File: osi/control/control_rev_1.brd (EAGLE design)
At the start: 25.4 x 25.4 mm, 8 parts, among them IC1 TINY24/44/84-PU

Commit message: control brain
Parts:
- removed C1: (no value), SparkFun:CAP-PTH-SMALL-KIT
- removed IC1: TINY24/44/84-PU, avr-7:DIL14
- removed IC2_L, IC2_R: (no value), SparkFun_mod:1X05
- removed U$1: PTS635_SWITCH, _my-parts:PTS635_SWITCH
- added C2: 100uF/6V, rcl-ez:E2,5-5
- added C6: 0.1uF, rcl-ez:C025-025X050
- added C7: 100uF/16V, rcl-ez:E2,5-6
- added J1, J2: 1X2-3.5MM, adafruit_mod:1X2-3.5MM
- added R2: (no value), adafruit_mod:0204V
- added TRACKS: L293D, texas:DIL16
- moved R1 6.35 mm to (14.0, 20.3), turned to 90 degrees
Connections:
- removed net D8: IC1.5, R1.1
- removed net RESET: IC1.4, U$1.P$2
- new net N$1: J1.2, TRACKS.3
- new net N$2: J2.2, TRACKS.14
- new net N$3: J1.1, TRACKS.6
- new net N$4: J2.1, TRACKS.11
- new net N$5: TRACKS.9
- new net N$6: R1.1
- new net N$7: R2.1
- new net VCC: C2.+, C6.1, TRACKS.16
- net +3V3: no longer C1.2, IC1.1, IC2_L.4, IC2_R.2
- net +5V: no longer IC2_L.5, IC2_R.1
- net AREF_D0: now also TRACKS.2; no longer IC1.13
- net D1: now also TRACKS.7; no longer IC1.12
- net D10: now also TRACKS.15; no longer IC1.2
- net D2: now also R2.2; no longer IC1.11
- net D3: now also R1.2; no longer IC1.10
- net D5: now also TRACKS.1; no longer IC1.8
- net D7: no longer IC1.6
- net D9: now also TRACKS.10; no longer IC1.3
- net GND: now also C2.-, C6.2, C7.-, TRACKS.12, TRACKS.13, TRACKS.4, TRACKS.5; no longer C1.1, IC1.14, IC2_L.3, IC2_R.3, R1.2, U$1.P$1
- net SCL_D4: no longer IC1.9, IC2_L.1, IC2_R.5
- net SDA_D6: no longer IC1.7, IC2_L.2, IC2_R.4
- net V+: now also C7.+, TRACKS.8
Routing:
- net +3V3: track 39.4 -> 0.00 mm
- net +5V: track 39.0 -> 0.00 mm
- net SDA_D6: track 37.0 -> 0.00 mm
- net SCL_D4: track 34.8 -> 0.00 mm
- net N$3: track 0.00 -> 26.3 mm
- net N$2: track 0.00 -> 21.8 mm
- net V+: track 0.00 -> 20.3 mm
- net VCC: track 0.00 -> 17.3 mm
- net D5: track 4.34 -> 20.9 mm
- net RESET: track 16.3 -> 0.00 mm
- net D7: track 14.1 -> 0.00 mm
- net D2: track 16.8 -> 3.07 mm
- net N$4: track 0.00 -> 13.6 mm
- net AREF_D0: track 25.9 -> 14.4 mm
- net D8: track 9.20 -> 0.00 mm
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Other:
- board text added: "CONTROL"
- board text added: "Control Rev 1 Feb 12"
- board text added: "L293D"
- board text removed: "3V3"
- board text removed: "Attiny 84"
- board text removed: "BRAIN"
- board text removed: "Brain Rev 1 Feb 12"
- board text removed: "RESET"
- board text removed: "SCK"
- board text removed: "SDA"

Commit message: update
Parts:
- added LED1, LED2: (no value), adafruit:LED3MM
- added R3, R4: (no value), adafruit_mod:0204V
- moved C6 1.97 mm to (22.9, 2.41)
- moved TRACKS 1.90 mm to (15.2, 8.89)
- moved C2 0.25 mm to (15.2, 16.3), turned to 90 degrees
- turned J1 to 180 degrees
- turned J2 to 180 degrees
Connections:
- net AREF_D0: now also LED1.A
- net D1: now also R3.1
- net D10: now also LED2.A
- net D9: now also R4.1
- net GND: now also R1.1, R2.1
- net N$1: now also J1.1; no longer J1.2
- net N$3: now also J1.2; no longer J1.1
- net N$6: now also LED1.K, R3.2; no longer R1.1
- net N$7: now also LED2.K, R4.2; no longer R2.1
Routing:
- net AREF_D0: track 14.4 -> 38.1 mm
- net N$7: track 0.00 -> 20.9 mm
- net D10: track 7.67 -> 24.4 mm
- net N$6: track 0.00 -> 11.3 mm
- net D9: track 6.40 -> 17.3 mm
- net V+: track 20.3 -> 27.1 mm
- net N$3: track 26.3 -> 21.9 mm
- net N$4: track 13.6 -> 17.2 mm
- net D5: track 20.9 -> 23.2 mm
- net D1: track 20.7 -> 19.6 mm
- net N$1: track 6.22 -> 5.19 mm
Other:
- board text added: "A"
- board text added: "B"
- board text added: "Rev 1 Feb 12"
- board text removed: "Control Rev 1 Feb 12"

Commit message: chuck
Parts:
- removed R1, R2: (no value), adafruit_mod:0204V
- moved JP8 1.27 mm to (6.35, 24.1)
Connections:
- removed net D2: JP8.6, R2.2
- removed net D3: JP8.5, R1.2
- net GND: now also JP8.5, JP8.6; no longer R1.1, R2.1
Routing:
- net D3: track 3.07 -> 0.00 mm
- net D2: track 3.07 -> 0.00 mm
- net AREF_D0: track 38.1 -> 38.8 mm
- net D5: track 23.2 -> 22.5 mm
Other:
- board text removed: "D4"
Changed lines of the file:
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@@
 <setting verticaltext="up"/>
 </settings>
-<grid distance="0.01" unitdist="inch" unit="inch" style="lines" multiple="1" display="yes" altdistance="0.005" altunitdist="inch" altunit="inch"/>
+<grid distance="0.05" unitdist="inch" unit="inch" style="lines" multiple="1" display="yes" altdistance="0.005" altunitdist="inch" altunit="inch"/>
 <layers>
 <layer number="1" name="Top" color="4" fill="1" visible="yes" active="yes"/>
@@
 <text x="12.192" y="2.413" size="1.016" layer="22" font="vector" ratio="15" rot="MR0">D9</text>
 <text x="15.367" y="2.413" size="1.016" layer="22" font="vector" ratio="15" rot="MR0">D10</text>
-<text x="23.622" y="21.971" size="1.016" layer="22" font="vector" ratio="15" rot="MR0">D0</text>
-<text x="21.082" y="21.971" size="1.016" layer="22" font="vector" ratio="15" rot="MR0">D1</text>
-<text x="18.923" y="21.971" size="1.016" layer="22" font="vector" ratio="15" rot="MR0">D2</text>
-<text x="16.002" y="22.098" size="1.016" layer="22" font="vector" ratio="15" rot="MR0">D3</text>
-<text x="13.081" y="21.971" size="1.016" layer="22" font="vector" ratio="15" rot="MR0">D4</text>
-<text x="10.922" y="21.971" size="1.016" layer="22" font="vector" ratio="15" rot="MR0">D5</text>
-<text x="8.382" y="21.971" size="1.016" layer="22" font="vector" ratio="15" rot="MR0">D6</text>
-<text x="5.842" y="21.971" size="1.016" layer="22" font="vector" ratio="15" rot="MR0">D7</text>
-<text x="4.191" y="21.59" size="1.016" layer="21" font="vector" ratio="15">D7</text>
-<text x="6.731" y="21.59" size="1.016" layer="21" font="vector" ratio="15">D6</text>
-<text x="9.271" y="21.59" size="1.016" layer="21" font="vector" ratio="15">D5</text>
-<text x="12.065" y="21.844" size="0.8128" layer="21" font="vector" ratio="15">D4</text>
-<text x="14.605" y="21.844" size="0.8128" layer="21" font="vector" ratio="15">D3</text>
-<text x="17.145" y="21.844" size="0.8128" layer="21" font="vector" ratio="15">D2</text>
-<text x="19.685" y="21.59" size="1.016" layer="21" font="vector" ratio="15">D1</text>
-<text x="22.098" y="21.59" size="1.016" layer="21" font="vector" ratio="15">D0</text>
+<text x="24.892" y="21.971" size="1.016" layer="22" font="vector" ratio="15" rot="MR0">D0</text>
+<text x="22.352" y="21.971" size="1.016" layer="22" font="vector" ratio="15" rot="MR0">D1</text>
+<text x="20.193" y="21.971" size="1.016" layer="22" font="vector" ratio="15" rot="MR0">D2</text>
+<text x="12.192" y="21.971" size="1.016" layer="22" font="vector" ratio="15" rot="MR0">D5</text>
+<text x="9.652" y="21.971" size="1.016" layer="22" font="vector" ratio="15" rot="MR0">D6</text>
+<text x="7.112" y="21.971" size="1.016" layer="22" font="vector" ratio="15" rot="MR0">D7</text>
+<text x="5.461" y="21.59" size="1.016" layer="21" font="vector" ratio="15">D7</text>
+<text x="8.001" y="21.59" size="1.016" layer="21" font="vector" ratio="15">D6</text>
+<text x="10.541" y="21.59" size="1.016" layer="21" font="vector" ratio="15">D5</text>
+<text x="15.875" y="21.844" size="0.8128" layer="21" font="vector" ratio="15">D3</text>
+<text x="18.415" y="21.844" size="0.8128" layer="21" font="vector" ratio="15">D2</text>
+<text x="20.955" y="21.59" size="1.016" layer="21" font="vector" ratio="15">D1</text>
+<text x="23.368" y="21.59" size="1.016" layer="21" font="vector" ratio="15">D0</text>
 <text x="0.508" y="2.794" size="1.016" layer="21" font="vector" ratio="15">V+</text>
 <text x="2.54" y="2.794" size="0.8128" layer="21" font="vector" ratio="15">GND</text>
@@
 <elements>
 <element name="JP6" library="SparkFun" package="1X06" value="" x="1.27" y="1.27"/>
-<element name="JP8" library="SparkFun" package="1X08" value="" x="5.08" y="24.13"/>
+<element name="JP8" library="SparkFun" package="1X08" value="" x="6.35" y="24.13"/>
 <element name="TRACKS" library="texas" package="DIL16" value="L293D" x="15.24" y="8.89" rot="R180"/>
 <element name="C7" library="rcl-ez" package="E2,5-6" value="100uF/16V" x="10.16" y="18.415"/>
@@
 <element name="J1" library="adafruit_mod" package="1X2-3.5MM" value="1X2-3.5MM" x="21.59" y="17.78" rot="R180"/>
 <element name="J2" library="adafruit_mod" package="1X2-3.5MM" value="1X2-3.5MM" x="3.81" y="17.78" rot="R180"/>
-<element name="R1" library="adafruit_mod" package="0204V" value="" x="13.97" y="20.32" rot="R90"/>
-<element name="R2" library="adafruit_mod" package="0204V" value="" x="16.51" y="20.32" rot="R90"/>
 <element name="LED1" library="adafruit" package="LED3MM" value="" x="2.54" y="12.065" rot="R90"/>
 <element name="LED2" library="adafruit" package="LED3MM" value="" x="2.54" y="7.366" rot="R90"/>
@@
 <contactref element="TRACKS" pad="5"/>
 <contactref element="TRACKS" pad="4"/>
-<contactref element="R1" pad="1"/>
-<contactref element="R2" pad="1"/>
+<contactref element="JP8" pad="5"/>
+<contactref element="JP8" pad="6"/>
 </signal>
 <signal name="SDA_D6">
@@
 <wire x1="6.35" y1="13.208" x2="6.35" y2="12.7" width="0.6096" layer="16"/>
 </signal>
-<signal name="D3">
-<contactref element="JP8" pad="5"/>
-<contactref element="R1" pad="2"/>
-<wire x1="15.24" y1="24.13" x2="15.24" y2="22.86" width="0.4064" layer="16"/>
-<wire x1="15.24" y1="22.86" x2="13.97" y2="21.59" width="0.4064" layer="16"/>
-</signal>
-<signal name="D2">
-<contactref element="JP8" pad="6"/>
-<contactref element="R2" pad="2"/>
-<wire x1="17.78" y1="24.13" x2="17.78" y2="22.86" width="0.4064" layer="16"/>
-<wire x1="17.78" y1="22.86" x2="16.51" y2="21.59" width="0.4064" layer="16"/>
-</signal>
 <signal name="D1">
 <contactref element="JP8" pad="7"/>
 <contactref element="TRACKS" pad="7"/>
-<wire x1="20.32" y1="24.13" x2="20.32" y2="21.59" width="0.3048" layer="16"/>
-<wire x1="20.32" y1="21.59" x2="18.034" y2="20.32" width="0.3048" layer="16"/>
+<wire x1="21.59" y1="24.13" x2="21.59" y2="23.495" width="0.3048" layer="16"/>
+<wire x1="21.59" y1="23.495" x2="18.034" y2="20.32" width="0.3048" layer="16"/>
 <wire x1="18.034" y1="20.32" x2="13.462" y2="20.32" width="0.3048" layer="16"/>
 <contactref element="R3" pad="1"/>
@@
 <contactref element="TRACKS" pad="2"/>
 <wire x1="21.59" y1="12.954" x2="21.59" y2="19.685" width="0.3048" layer="16"/>
-<wire x1="21.59" y1="19.685" x2="22.86" y2="20.955" width="0.3048" layer="16"/>
-<wire x1="22.86" y1="20.955" x2="22.86" y2="24.13" width="0.3048" layer="16"/>
+<wire x1="21.59" y1="19.685" x2="24.13" y2="21.59" width="0.3048" layer="16"/>
+<wire x1="24.13" y1="21.59" x2="24.13" y2="24.13" width="0.3048" layer="16"/>
 <contactref element="LED1" pad="A"/>
 <wire x1="2.54" y1="10.795" x2="3.429" y2="9.906" width="0.3048" layer="16"/>
@@
 <contactref element="TRACKS" pad="1"/>
 <wire x1="23.495" y1="20.32" x2="13.335" y2="20.32" width="0.3048" layer="1"/>
-<wire x1="13.335" y1="20.32" x2="10.16" y2="24.13" width="0.3048" layer="1"/>
+<wire x1="13.335" y1="20.32" x2="11.43" y2="24.13" width="0.3048" layer="1"/>
 <wire x1="23.495" y1="20.32" x2="24.765" y2="18.415" width="0.3048" layer="1"/>
 <wire x1="24.765" y1="18.415" x2="24.765" y2="15.24" width="0.3048" layer="1"/>

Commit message: control
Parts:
- added JP1: (no value), adafruit_mod:1X03
- moved LED1 13.7 mm to (15.9, 15.2), turned to 180 degrees
- moved LED2 10.7 mm to (9.78, 15.2), turned to 0 degrees
- moved C2 3.86 mm to (15.9, 20.1)
- moved R3 2.33 mm to (12.8, 16.1), turned to 270 degrees
- moved C7 1.65 mm to (10.2, 20.1)
- moved R4 1.27 mm to (17.8, 1.02)
- moved C6 1.27 mm to (22.9, 1.14)
- moved TRACKS 0.63 mm to (15.2, 8.26)
- moved J1 0.51 mm to (22.1, 17.8)
- moved J2 0.18 mm to (3.68, 17.9)
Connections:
- new net N$8: C7.+, JP1.2, TRACKS.8
- net +5V: now also JP1.1
- net V+: now also JP1.3; no longer C7.+, TRACKS.8
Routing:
- net AREF_D0: track 38.8 -> 18.7 mm
- net V+: track 27.1 -> 12.2 mm
- net N$8: track 0.00 -> 13.9 mm
- net N$6: track 11.3 -> 1.94 mm
- net +5V: track 0.00 -> 6.23 mm
- net D10: track 24.4 -> 29.1 mm
- net VCC: track 17.4 -> 21.4 mm
- net N$7: track 20.9 -> 18.7 mm
- net D5: track 22.5 -> 21.1 mm
- net D9: track 17.3 -> 18.4 mm
- net N$1: track 5.19 -> 6.29 mm
- net N$4: track 17.2 -> 18.2 mm
- net N$2: track 21.4 -> 22.1 mm
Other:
- board text added: "D4"
- board text removed: "One Square Inch"

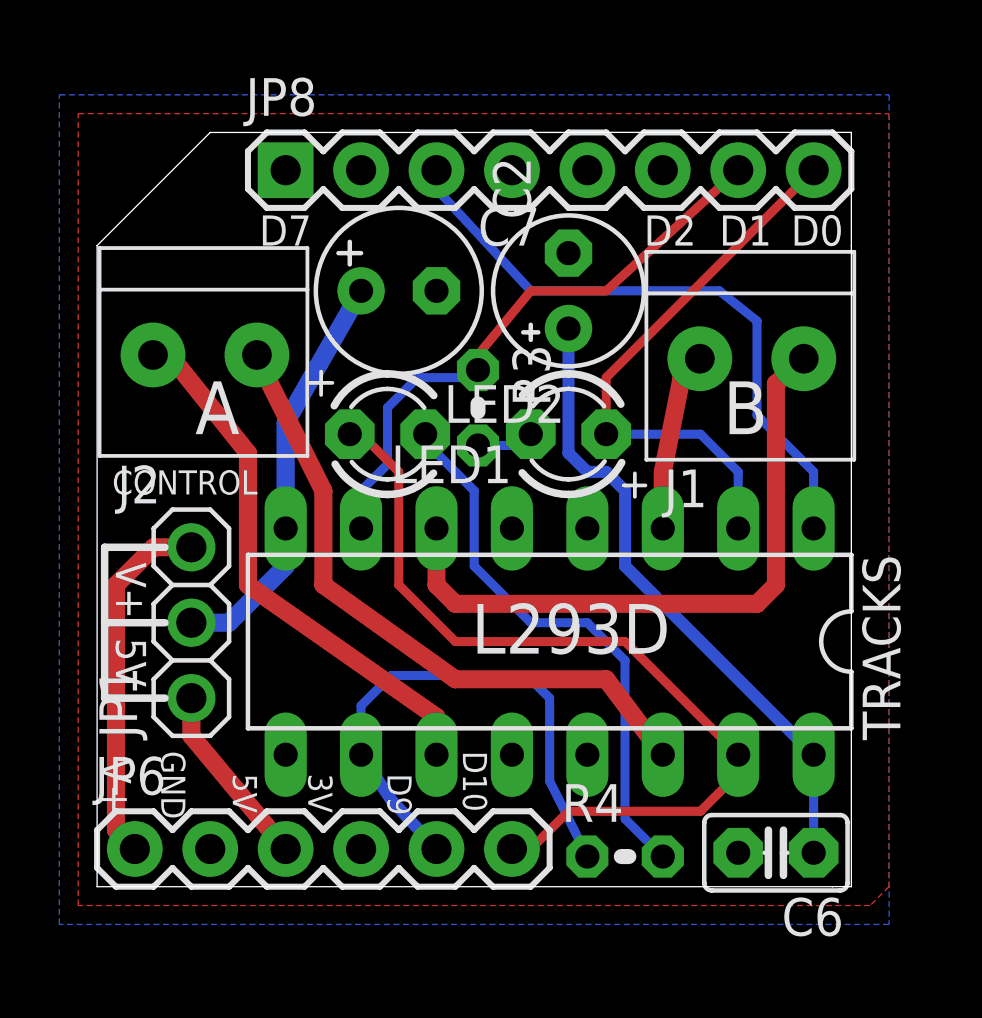
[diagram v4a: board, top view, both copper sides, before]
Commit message: D9 -> D8 for INT0
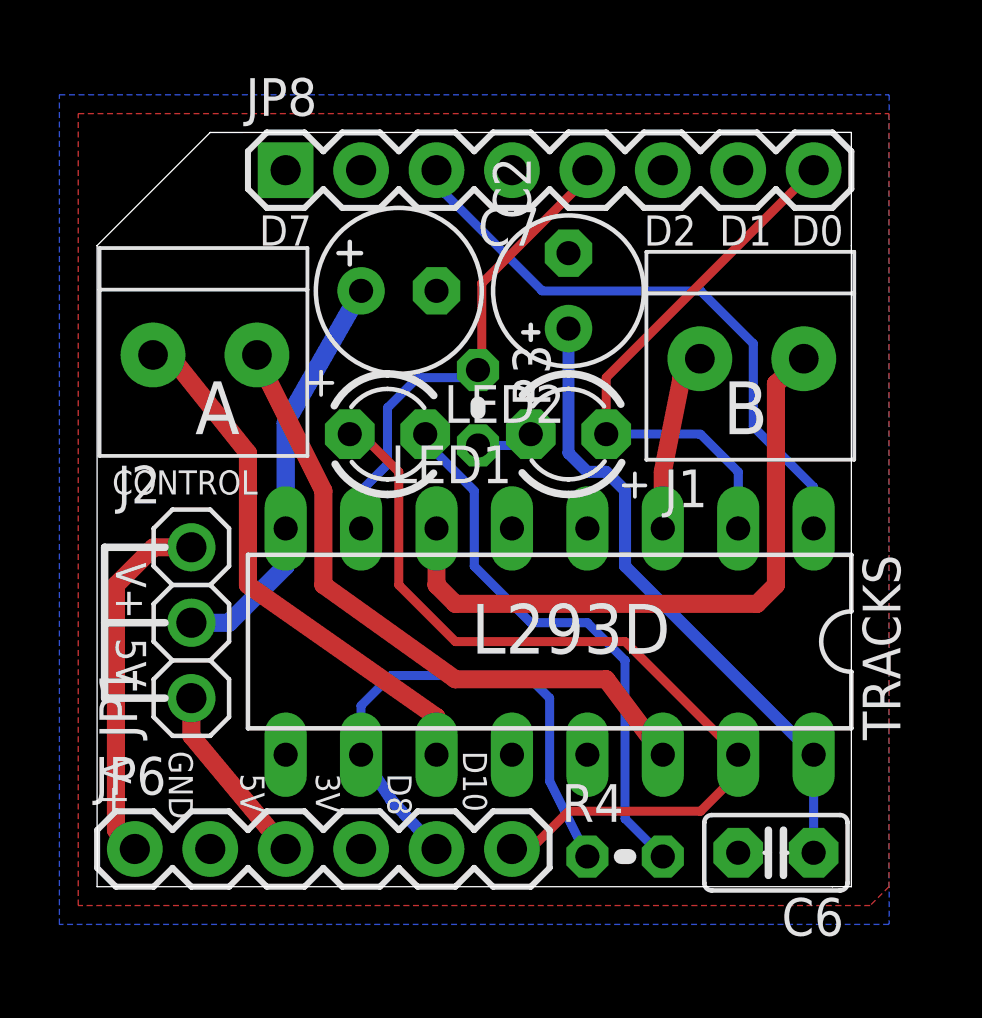
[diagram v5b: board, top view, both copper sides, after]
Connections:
- net D9 renamed D8
- new net D2: JP8.6
- new net D3: JP8.5, R3.1, TRACKS.7
- net D1: no longer R3.1, TRACKS.7
- net GND: no longer JP8.5, JP8.6
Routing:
- net D1: track 19.9 -> 0.00 mm
- net D3: track 0.00 -> 16.3 mm
- net D5: track 21.1 -> 20.5 mm
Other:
- board text added: "D8"
- board text removed: "D9"
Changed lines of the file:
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@@
 <grid distance="0.01" unitdist="inch" unit="inch" style="lines" multiple="1" display="yes" altdistance="0.005" altunitdist="inch" altunit="inch"/>
 <layers>
-<layer number="1" name="Top" color="4" fill="1" visible="no" active="yes"/>
-<layer number="16" name="Bottom" color="1" fill="1" visible="no" active="yes"/>
+<layer number="1" name="Top" color="4" fill="1" visible="yes" active="yes"/>
+<layer number="16" name="Bottom" color="1" fill="1" visible="yes" active="yes"/>
 <layer number="17" name="Pads" color="2" fill="1" visible="yes" active="yes"/>
 <layer number="18" name="Vias" color="2" fill="1" visible="yes" active="yes"/>
@@
 <text x="19.304" y="9.525" size="1.6764" layer="21" font="vector" ratio="10" rot="R180">L293D</text>
 <text x="24.892" y="6.35" size="1.016" layer="22" font="vector" ratio="15" rot="MR0">MakersBox.blogspot.com</text>
-<text x="23.622" y="19.05" size="1.016" layer="22" font="vector" ratio="12" rot="MR0">Rev 1
+<text x="11.684" y="7.62" size="1.016" layer="22" font="vector" ratio="12" rot="MR0">Rev 1
 Feb 12</text>
 <text x="1.397" y="2.54" size="0.8128" layer="22" font="vector" ratio="15" rot="MR90">V+</text>
@@
 <text x="6.985" y="2.286" size="0.8128" layer="22" font="vector" ratio="15" rot="MR90">5V</text>
 <text x="9.525" y="2.286" size="0.8128" layer="22" font="vector" ratio="15" rot="MR90">3V</text>
-<text x="12.065" y="2.286" size="0.8128" layer="22" font="vector" ratio="15" rot="MR90">D9</text>
+<text x="12.065" y="2.286" size="0.8128" layer="22" font="vector" ratio="15" rot="MR90">D8</text>
 <text x="14.859" y="2.159" size="0.8128" layer="22" font="vector" ratio="15" rot="MR90">D10</text>
 <text x="24.892" y="21.971" size="1.016" layer="22" font="vector" ratio="15" rot="MR0">D0</text>
@@
 <text x="23.368" y="21.59" size="1.016" layer="21" font="vector" ratio="15">D0</text>
 <text x="0.127" y="4.318" size="1.016" layer="21" font="vector" ratio="15" rot="SR270">V+</text>
-<text x="2.159" y="4.572" size="0.8128" layer="21" font="vector" ratio="15" rot="SR270">GND</text>
-<text x="4.572" y="3.81" size="0.8128" layer="21" font="vector" ratio="15" rot="SR270">5V</text>
-<text x="7.112" y="3.81" size="0.8128" layer="21" font="vector" ratio="15" rot="SR270">3V</text>
-<text x="9.779" y="3.81" size="0.8128" layer="21" font="vector" ratio="15" rot="SR270">D9</text>
+<text x="2.413" y="4.572" size="0.8128" layer="21" font="vector" ratio="15" rot="SR270">GND</text>
+<text x="4.826" y="3.81" size="0.8128" layer="21" font="vector" ratio="15" rot="SR270">5V</text>
+<text x="7.366" y="3.81" size="0.8128" layer="21" font="vector" ratio="15" rot="SR270">3V</text>
+<text x="9.779" y="3.81" size="0.8128" layer="21" font="vector" ratio="15" rot="SR270">D8</text>
 <text x="12.319" y="4.572" size="0.8128" layer="21" font="vector" ratio="15" rot="SR270">D10</text>
 <text x="24.638" y="8.128" size="1.778" layer="22" font="vector" ratio="15" rot="MR0">CONTROL</text>
@@
 <contactref element="TRACKS" pad="5"/>
 <contactref element="TRACKS" pad="4"/>
-<contactref element="JP8" pad="5"/>
-<contactref element="JP8" pad="6"/>
 </signal>
 <signal name="SDA_D6">
@@
 <wire x1="3.175" y1="5.08" x2="3.175" y2="6.35" width="0.6096" layer="1"/>
 </signal>
-<signal name="D9">
+<signal name="D8">
 <contactref element="JP6" pad="5"/>
 <contactref element="TRACKS" pad="10"/>
@@
 <wire x1="0.635" y1="1.905" x2="1.27" y2="1.27" width="0.6096" layer="1"/>
 </signal>
-<signal name="D1">
-<contactref element="JP8" pad="7"/>
+<signal name="D3">
 <contactref element="TRACKS" pad="7"/>
 <contactref element="R3" pad="1"/>
@@
 <wire x1="10.795" y1="17.145" x2="12.573" y2="17.145" width="0.3048" layer="16"/>
 <wire x1="12.573" y1="17.145" x2="12.827" y2="17.399" width="0.3048" layer="16"/>
-<wire x1="12.827" y1="17.399" x2="12.827" y2="17.907" width="0.3048" layer="1"/>
-<wire x1="12.827" y1="17.907" x2="14.605" y2="20.066" width="0.3048" layer="1"/>
-<wire x1="14.605" y1="20.066" x2="17.145" y2="20.066" width="0.3048" layer="1"/>
-<wire x1="17.145" y1="20.066" x2="21.59" y2="24.13" width="0.3048" layer="1"/>
+<contactref element="JP8" pad="5"/>
+<wire x1="16.51" y1="24.13" x2="16.51" y2="23.876" width="0.3048" layer="1"/>
+<wire x1="16.51" y1="23.876" x2="12.954" y2="20.32" width="0.3048" layer="1"/>
+<wire x1="12.954" y1="20.32" x2="12.954" y2="17.526" width="0.3048" layer="1"/>
+<wire x1="12.954" y1="17.526" x2="12.827" y2="17.399" width="0.3048" layer="1"/>
 </signal>
 <signal name="AREF_D0">
@@
 <contactref element="JP8" pad="3"/>
 <contactref element="TRACKS" pad="1"/>
-<wire x1="11.43" y1="24.13" x2="11.43" y2="23.495" width="0.3048" layer="16"/>
-<wire x1="11.43" y1="23.495" x2="14.605" y2="20.066" width="0.3048" layer="16"/>
-<wire x1="14.605" y1="20.066" x2="20.955" y2="20.066" width="0.3048" layer="16"/>
-<wire x1="20.955" y1="20.066" x2="22.225" y2="19.05" width="0.3048" layer="16"/>
-<wire x1="22.225" y1="19.05" x2="22.225" y2="15.875" width="0.3048" layer="16"/>
-<wire x1="22.225" y1="15.875" x2="24.13" y2="13.97" width="0.3048" layer="16"/>
-<wire x1="24.13" y1="13.97" x2="24.13" y2="12.065" width="0.3048" layer="16"/>
+<wire x1="24.13" y1="12.065" x2="24.13" y2="13.462" width="0.3048" layer="16"/>
+<wire x1="24.13" y1="13.462" x2="22.098" y2="15.494" width="0.3048" layer="16"/>
+<wire x1="22.098" y1="15.494" x2="22.098" y2="18.288" width="0.3048" layer="16"/>
+<wire x1="22.098" y1="18.288" x2="20.32" y2="20.066" width="0.3048" layer="16"/>
+<wire x1="20.32" y1="20.066" x2="14.986" y2="20.066" width="0.3048" layer="16"/>
+<wire x1="14.986" y1="20.066" x2="11.43" y2="23.622" width="0.3048" layer="16"/>
+<wire x1="11.43" y1="23.622" x2="11.43" y2="24.13" width="0.3048" layer="16"/>
 </signal>
 <signal name="D7">
@@
 <wire x1="4.445" y1="8.89" x2="3.175" y2="8.89" width="0.6096" layer="16"/>
 </signal>
+<signal name="D1">
+<contactref element="JP8" pad="7"/>
+</signal>
+<signal name="D2">
+<contactref element="JP8" pad="6"/>
+</signal>
 </signals>
